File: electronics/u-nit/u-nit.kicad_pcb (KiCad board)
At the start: 2 copper layers, 65 x 80 mm, 82 parts, among them J1 TBP02R2-381-02BE, J10 TBP02R2-381-04BE, J11 TBP02R2-381-04BE, J12 TBP02R2-381-03BE, J2 PJ-002A, J3 Conn_ARM_JTAG_SWD_10, J4 Conn_01x05_Socket, J5 TBP02R2-381-04BE, J6 TBP02R2-381-03BE, J7 TBP02R2-381-04BE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

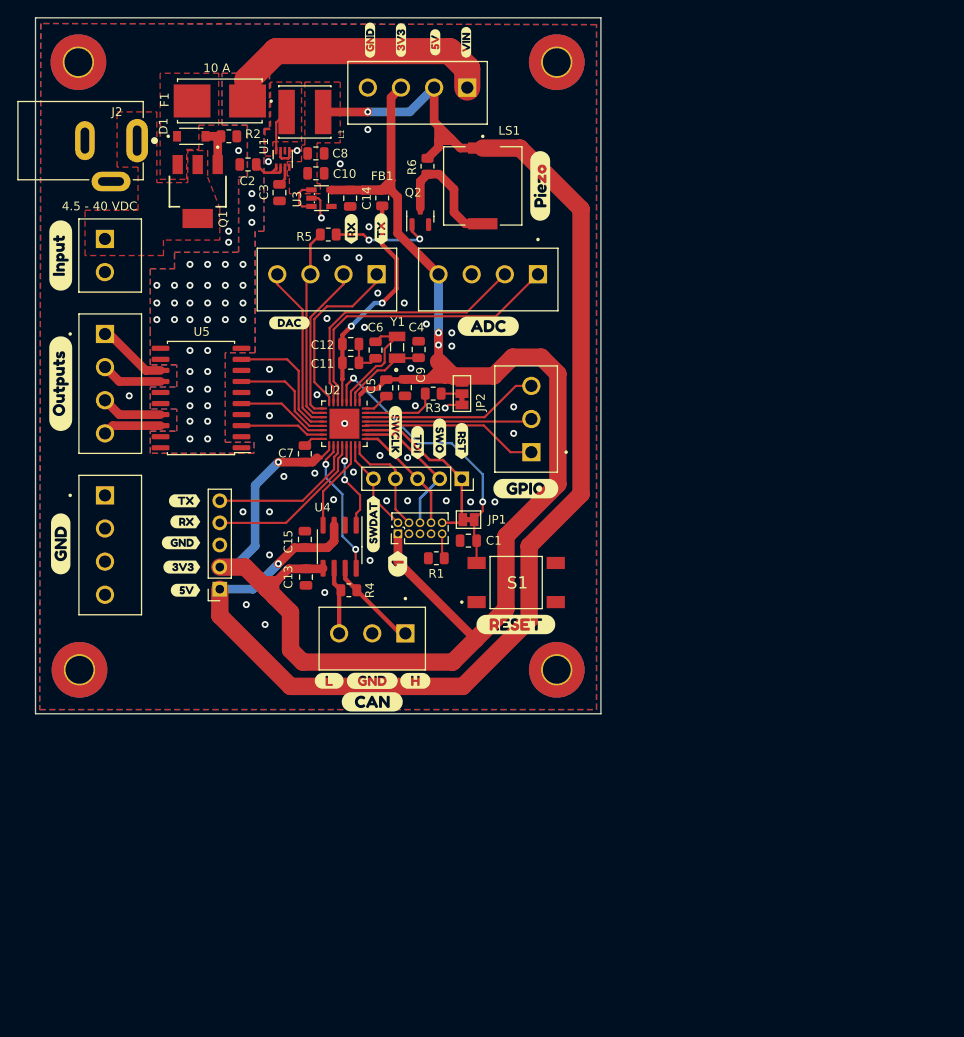
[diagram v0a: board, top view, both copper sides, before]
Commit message: exported PCB step and created base container
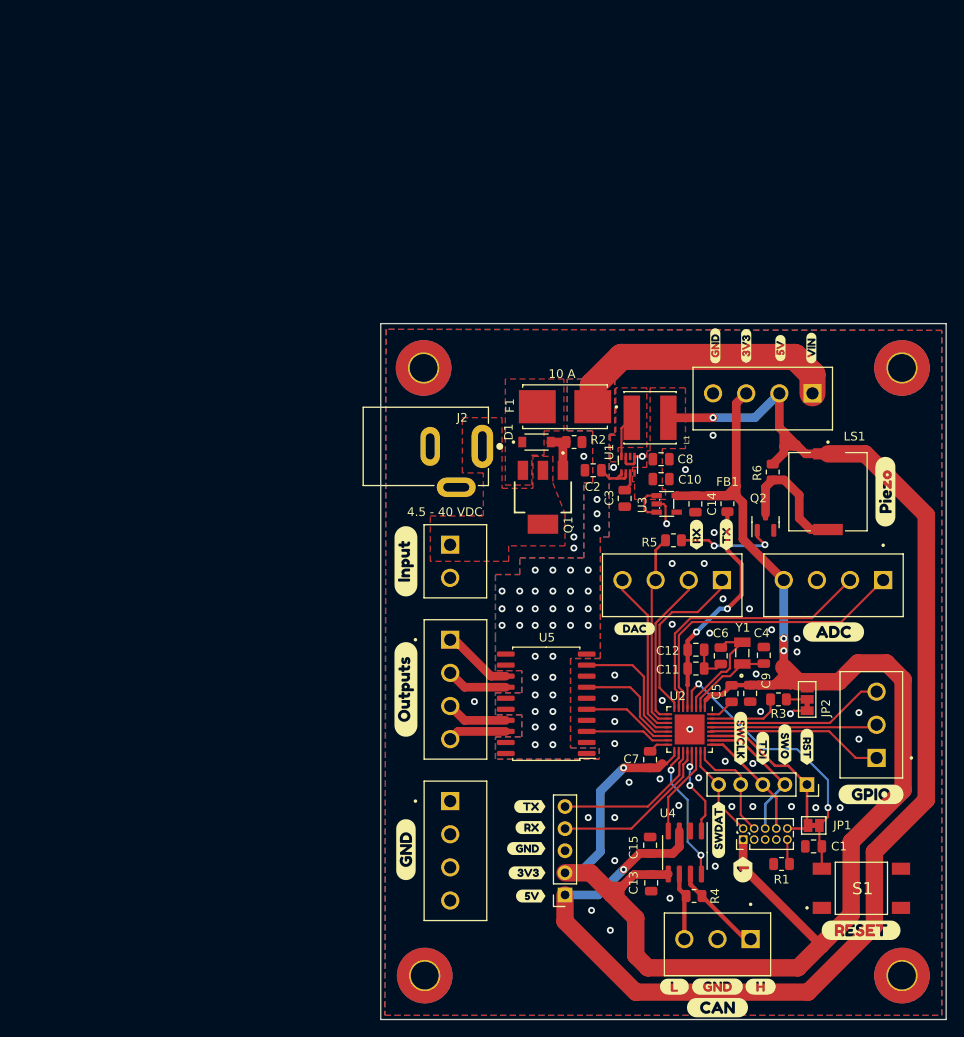
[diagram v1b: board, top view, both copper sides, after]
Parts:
- moved C1 53.0 mm to (159.4, 120.3)
- moved C10 53.0 mm to (141.9, 78.0)
- moved C6 53.0 mm to (148.8, 98.3)
- moved C8 53.0 mm to (141.9, 75.7)
- moved H2 53.0 mm to (169.6, 65.2)
- moved J4 53.0 mm to (158.7, 113.1)
- moved U2 53.0 mm to (145.2, 106.8)
- moved U4 53.0 mm to (144.6, 121.0)
- moved kibuzzard-64E9EAC2 53.0 mm to (155.6, 63.0)
- moved kibuzzard-64E9EBA4 53.0 mm to (161.7, 95.6)
- moved kibuzzard-64E9EC55 53.0 mm to (158.7, 108.8)
- moved C13 53.0 mm to (140.8, 124.4)
- moved C14 53.0 mm to (145.9, 80.9)
- moved C2 53.0 mm to (134.1, 77.0)
- moved C3 53.0 mm to (137.7, 80.2)
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
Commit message: added digikey BOM, schematic (pdf) and gerber files
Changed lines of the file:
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@@
   )
   (paper "A4")
+  (title_block
+    (title "U-NIT")
+    (date "2023-08-27")
+    (rev "1.0")
+    (company "Harvey Bates")
+  )
   (layers
     (0 "F.Cu" signal)
@@
       (outputformat 1)
       (mirror false)
-      (drillshape 1)
+      (drillshape 0)
       (scaleselection 1)
-      (outputdirectory "")
+      (outputdirectory "gerber/")
     )
   )
@@
     (fp_line (start 1 0.625) (end -1 0.625)
       (stroke (width 0.1) (type solid)) (layer "F.Fab"))
-    (pad "1" smd roundrect (at -0.9125 0 180) (size 1.025 1.4) (layers "F.Cu" "F.Paste" "F.Mask") (roundrect_rratio 0.243902)
+    (pad "1" smd roundrect (at -0.9125 0 180) (size 1.025 1.4) (layers "F.Cu" "F.Paste" "F.Mask") (roundrect_rratio 0.243902439)
       (net 17 "Net-(J3-GNDDetect)") (pintype "passive"))
-    (pad "2" smd roundrect (at 0.9125 0 180) (size 1.025 1.4) (layers "F.Cu" "F.Paste" "F.Mask") (roundrect_rratio 0.243902)
+    (pad "2" smd roundrect (at 0.9125 0 180) (size 1.025 1.4) (layers "F.Cu" "F.Paste" "F.Mask") (roundrect_rratio 0.243902439)
       (net 2 "GND") (pintype "passive"))
     (model "${KICAD6_3DMODEL_DIR}/Resistor_SMD.3dshapes/R_0805_2012Metric.wrl"
@@
     (fp_line (start 1 0.625) (end -1 0.625)
       (stroke (width 0.1) (type solid)) (layer "F.Fab"))
-    (pad "1" smd roundrect (at -0.9125 0 180) (size 1.025 1.4) (layers "F.Cu" "F.Paste" "F.Mask") (roundrect_rratio 0.243902)
+    (pad "1" smd roundrect (at -0.9125 0 180) (size 1.025 1.4) (layers "F.Cu" "F.Paste" "F.Mask") (roundrect_rratio 0.243902439)
       (net 34 "Net-(U4-CANH)") (pintype "passive"))
-    (pad "2" smd roundrect (at 0.9125 0 180) (size 1.025 1.4) (layers "F.Cu" "F.Paste" "F.Mask") (roundrect_rratio 0.243902)
+    (pad "2" smd roundrect (at 0.9125 0 180) (size 1.025 1.4) (layers "F.Cu" "F.Paste" "F.Mask") (roundrect_rratio 0.243902439)
       (net 35 "Net-(U4-CANL)") (pintype "passive"))
     (model "${KICAD6_3DMODEL_DIR}/Resistor_SMD.3dshapes/R_0805_2012Metric.wrl"
@@
     (fp_line (start 1 0.625) (end -1 0.625)
       (stroke (width 0.1) (type solid)) (layer "F.Fab"))
-    (pad "1" smd roundrect (at -0.9125 0 90) (size 1.025 1.4) (layers "F.Cu" "F.Paste" "F.Mask") (roundrect_rratio 0.243902)
+    (pad "1" smd roundrect (at -0.9125 0 90) (size 1.025 1.4) (layers "F.Cu" "F.Paste" "F.Mask") (roundrect_rratio 0.243902439)
       (net 9 "VDDA") (pintype "passive"))
-    (pad "2" smd roundrect (at 0.9125 0 90) (size 1.025 1.4) (layers "F.Cu" "F.Paste" "F.Mask") (roundrect_rratio 0.243902)
+    (pad "2" smd roundrect (at 0.9125 0 90) (size 1.025 1.4) (layers "F.Cu" "F.Paste" "F.Mask") (roundrect_rratio 0.243902439)
       (net 6 "+3.3V") (pintype "passive"))
     (model "${KICAD6_3DMODEL_DIR}/Resistor_SMD.3dshapes/R_0805_2012Metric.wrl"
@@
     (fp_line (start 1 0.625) (end -1 0.625)
       (stroke (width 0.1) (type solid)) (layer "F.Fab"))
-    (pad "1" smd roundrect (at -0.9125 0 180) (size 1.025 1.4) (layers "F.Cu" "F.Paste" "F.Mask") (roundrect_rratio 0.243902)
+    (pad "1" smd roundrect (at -0.9125 0 180) (size 1.025 1.4) (layers "F.Cu" "F.Paste" "F.Mask") (roundrect_rratio 0.243902439)
       (net 36 "Net-(JP2-C)") (pintype "passive"))
-    (pad "2" smd roundrect (at 0.9125 0 180) (size 1.025 1.4) (layers "F.Cu" "F.Paste" "F.Mask") (roundrect_rratio 0.243902)
+    (pad "2" smd roundrect (at 0.9125 0 180) (size 1.025 1.4) (layers "F.Cu" "F.Paste" "F.Mask") (roundrect_rratio 0.243902439)
       (net 41 "/BOOT_SELECT") (pintype "passive"))
     (model "${KICAD6_3DMODEL_DIR}/Resistor_SMD.3dshapes/R_0805_2012Metric.wrl"
@@
     (fp_line (start 1 0.625) (end -1 0.625)
       (stroke (width 0.1) (type solid)) (layer "F.Fab"))
-    (pad "1" smd roundrect (at -0.9125 0 180) (size 1.025 1.4) (layers "F.Cu" "F.Paste" "F.Mask") (roundrect_rratio 0.243902)
+    (pad "1" smd roundrect (at -0.9125 0 180) (size 1.025 1.4) (layers "F.Cu" "F.Paste" "F.Mask") (roundrect_rratio 0.243902439)
       (net 2 "GND") (pintype "passive"))
-    (pad "2" smd roundrect (at 0.9125 0 180) (size 1.025 1.4) (layers "F.Cu" "F.Paste" "F.Mask") (roundrect_rratio 0.243902)
+    (pad "2" smd roundrect (at 0.9125 0 180) (size 1.025 1.4) (layers "F.Cu" "F.Paste" "F.Mask") (roundrect_rratio 0.243902439)
       (net 39 "Net-(D1-A)") (pintype "passive"))
     (model "${KICAD6_3DMODEL_DIR}/Resistor_SMD.3dshapes/R_0805_2012Metric.wrl"
@@
     (fp_line (start 1 0.625) (end -1 0.625)
       (stroke (width 0.1) (type solid)) (layer "F.Fab"))
-    (pad "1" smd roundrect (at -0.9125 0) (size 1.025 1.4) (layers "F.Cu" "F.Paste" "F.Mask") (roundrect_rratio 0.243902)
+    (pad "1" smd roundrect (at -0.9125 0) (size 1.025 1.4) (layers "F.Cu" "F.Paste" "F.Mask") (roundrect_rratio 0.243902439)
       (net 26 "/DAC1_OUT1") (pintype "passive"))
-    (pad "2" smd roundrect (at 0.9125 0) (size 1.025 1.4) (layers "F.Cu" "F.Paste" "F.Mask") (roundrect_rratio 0.243902)
+    (pad "2" smd roundrect (at 0.9125 0) (size 1.025 1.4) (layers "F.Cu" "F.Paste" "F.Mask") (roundrect_rratio 0.243902439)
       (net 40 "Net-(Q2-B)") (pintype "passive"))
     (model "${KICAD6_3DMODEL_DIR}/Resistor_SMD.3dshapes/R_0805_2012Metric.wrl"
@@
     (fp_line (start 1 0.625) (end -1 0.625)
       (stroke (width 0.1) (type solid)) (layer "F.Fab"))
-    (pad "1" smd roundrect (at -0.9125 0 90) (size 1.025 1.4) (layers "F.Cu" "F.Paste" "F.Mask") (roundrect_rratio 0.243902)
+    (pad "1" smd roundrect (at -0.9125 0 90) (size 1.025 1.4) (layers "F.Cu" "F.Paste" "F.Mask") (roundrect_rratio 0.243902439)
       (net 38 "Net-(Q2-C)") (pintype "passive"))
-    (pad "2" smd roundrect (at 0.9125 0 90) (size 1.025 1.4) (layers "F.Cu" "F.Paste" "F.Mask") (roundrect_rratio 0.243902)
+    (pad "2" smd roundrect (at 0.9125 0 90) (size 1.025 1.4) (layers "F.Cu" "F.Paste" "F.Mask") (roundrect_rratio 0.243902439)
       (net 8 "+5V") (pintype "passive"))
     (model "${KICAD6_3DMODEL_DIR}/Resistor_SMD.3dshapes/R_0805_2012Metric.wrl"

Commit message: added gerber for lid and finalised gerber for both lid and PCB
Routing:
- net +5V: track 161.1 -> 165.3 mm
- net GND: vias 48 -> 51
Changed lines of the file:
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@@
   (via (at 146.239019 112.365596) (size 0.8) (drill 0.4) (layers "F.Cu" "B.Cu") (free) (net 2))
   (via (at 159.701019 115.794596) (size 0.8) (drill 0.4) (layers "F.Cu" "B.Cu") (free) (net 2))
+  (via (at 172.466 127.381) (size 0.8) (drill 0.4) (layers "F.Cu" "B.Cu") (free) (net 2))
   (via (at 143.191019 87.727596) (size 0.8) (drill 0.4) (layers "F.Cu" "B.Cu") (free) (net 2))
   (via (at 152.081019 92.934596) (size 0.8) (drill 0.4) (layers "F.Cu" "B.Cu") (free) (net 2))
@@
   (via (at 153.351019 104.745596) (size 0.8) (drill 0.4) (layers "F.Cu" "B.Cu") (free) (net 2))
   (via (at 152.843019 100.427596) (size 0.8) (drill 0.4) (layers "F.Cu" "B.Cu") (free) (net 2))
+  (via (at 170.561 130.048) (size 0.8) (drill 0.4) (layers "F.Cu" "B.Cu") (free) (net 2))
   (via (at 136.587019 121.890596) (size 0.8) (drill 0.4) (layers "F.Cu" "B.Cu") (free) (net 2))
   (via (at 164.654019 104.872596) (size 0.8) (drill 0.4) (layers "F.Cu" "B.Cu") (free) (net 2))
+  (via (at 155.956 130.937) (size 0.8) (drill 0.4) (layers "F.Cu" "B.Cu") (free) (net 2))
   (via (at 147.509019 95.728596) (size 0.8) (drill 0.4) (layers "F.Cu" "B.Cu") (free) (net 2))
   (via (at 157.542019 97.887596) (size 0.8) (drill 0.4) (layers "F.Cu" "B.Cu") (free) (net 2))
@@
   (segment (start 156.018019 72.614596) (end 156.018019 74.265596) (width 1) (layer "F.Cu") (net 8))
   (segment (start 140.651019 121.062596) (end 143.257019 121.062596) (width 1) (layer "F.Cu") (net 8))
+  (segment (start 158.526019 75.122596) (end 155.510019 72.106596) (width 2) (layer "F.Cu") (net 8))
   (segment (start 140.320519 79.930096) (end 140.016019 80.234596) (width 0.25) (layer "F.Cu") (net 8))
-  (segment (start 158.526019 75.122596) (end 161.098019 75.122596) (width 1) (layer "F.Cu") (net 8))
   (segment (start 142.751019 70.974096) (end 147.879519 70.974096) (width 1) (layer "F.Cu") (net 8))
+  (segment (start 161.098019 75.122596) (end 158.526019 75.122596) (width 2) (layer "F.Cu") (net 8))
   (segment (start 172.401019 114.905596) (end 166.432019 120.874596) (width 2) (layer "F.Cu") (net 8))
   (segment (start 157.478519 74.075096) (end 158.526019 75.122596) (width 1) (layer "F.Cu") (net 8))
@@
   (segment (start 165.384019 75.122596) (end 172.401019 82.139596) (width 2) (layer "F.Cu") (net 8))
   (segment (start 156.018019 72.614596) (end 157.478519 74.075096) (width 1) (layer "F.Cu") (net 8))
-  (segment (start 155.510019 68.169596) (end 155.510019 72.106596) (width 1) (layer "F.Cu") (net 8))
   (segment (start 157.478519 74.075096) (end 157.288019 74.265596) (width 1) (layer "F.Cu") (net 8))
   (segment (start 139.447019 121.062596) (end 140.651019 121.062596) (width 1) (layer "F.Cu") (net 8))
@@
   (segment (start 143.257019 121.062596) (end 144.014019 120.305596) (width 1) (layer "F.Cu") (net 8))
   (segment (start 161.098019 75.122596) (end 165.384019 75.122596) (width 2) (layer "F.Cu") (net 8))
+  (segment (start 155.510019 72.106596) (end 155.510019 68.169596) (width 2) (layer "F.Cu") (net 8))
   (via (at 147.890019 70.963596) (size 0.8) (drill 0.4) (layers "F.Cu" "B.Cu") (net 8))
   (via (at 137.603019 122.906596) (size 0.8) (drill 0.4) (layers "F.Cu" "B.Cu") (net 8))
